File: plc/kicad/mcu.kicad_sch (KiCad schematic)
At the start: 26 parts, among them Q3 L8050QLT1G, Q4 L8050QLT1G, SW1 TSD003B08026A03, SW2 TSD003B08026A03, U10 CP2102N-A02-GQFN28R, U9 ESP32-S3-MINI-1U

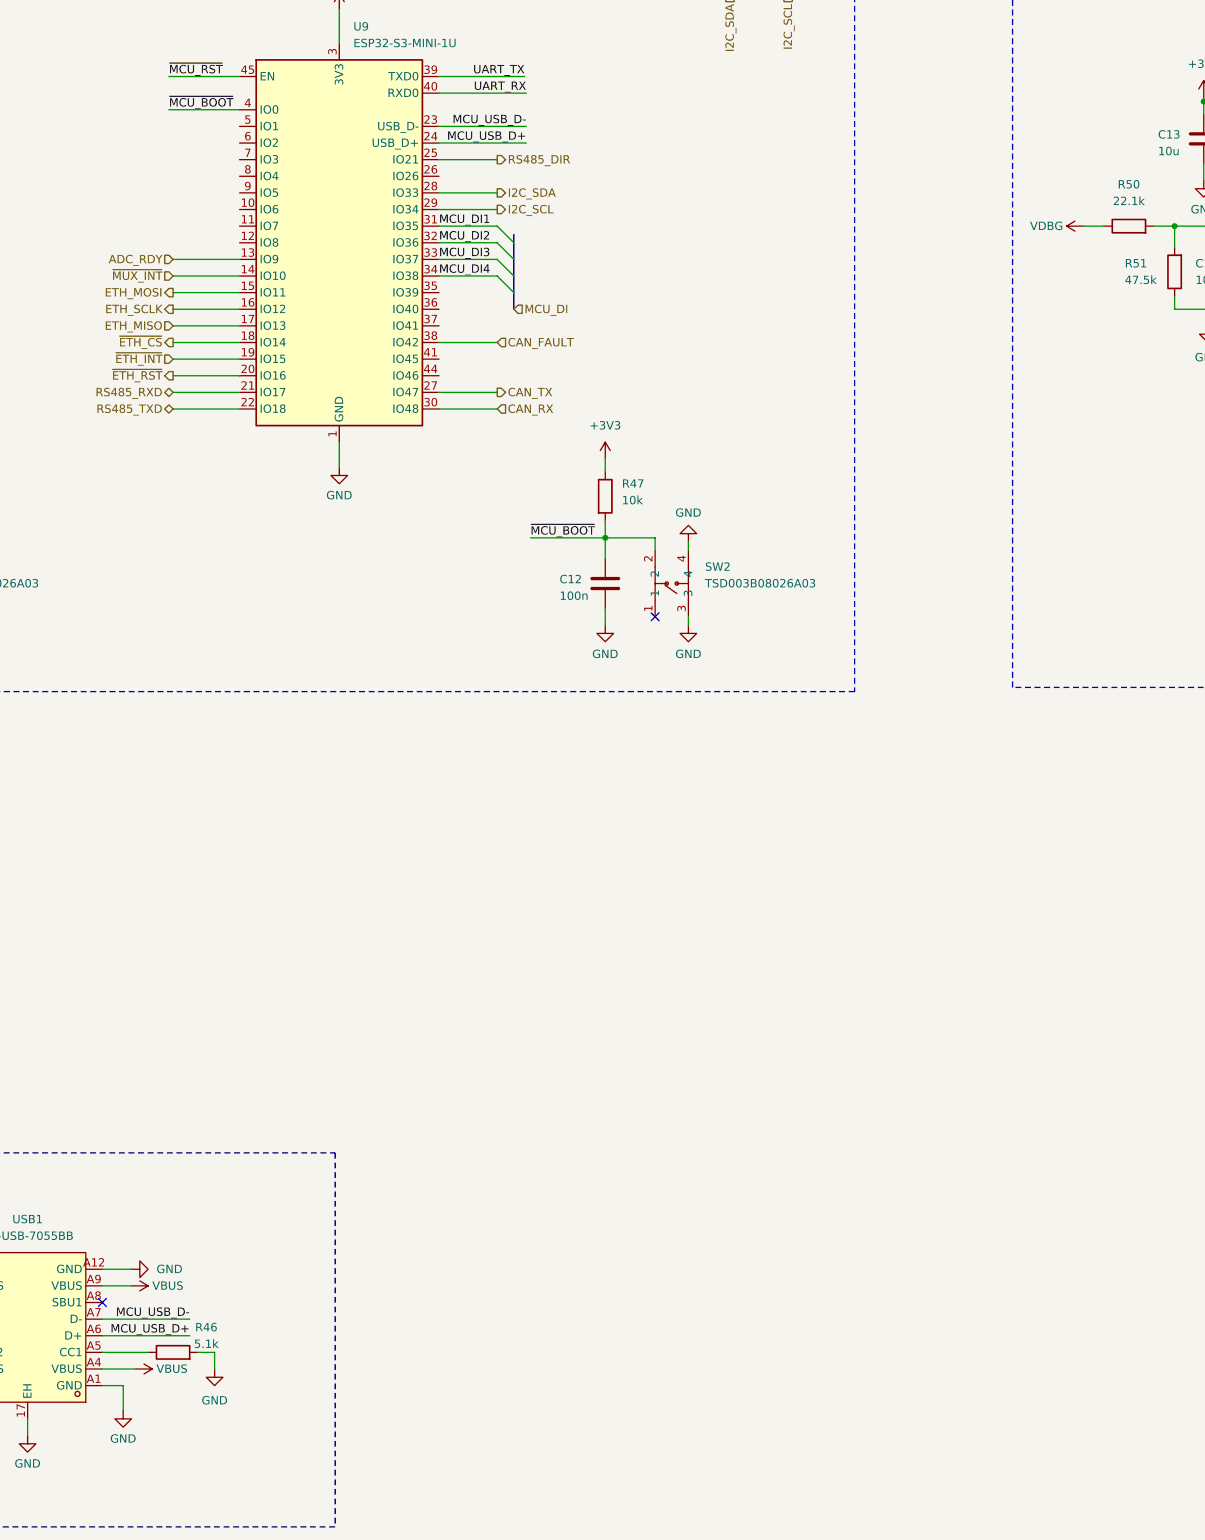
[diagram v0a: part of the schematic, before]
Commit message: AHT20 sensor added
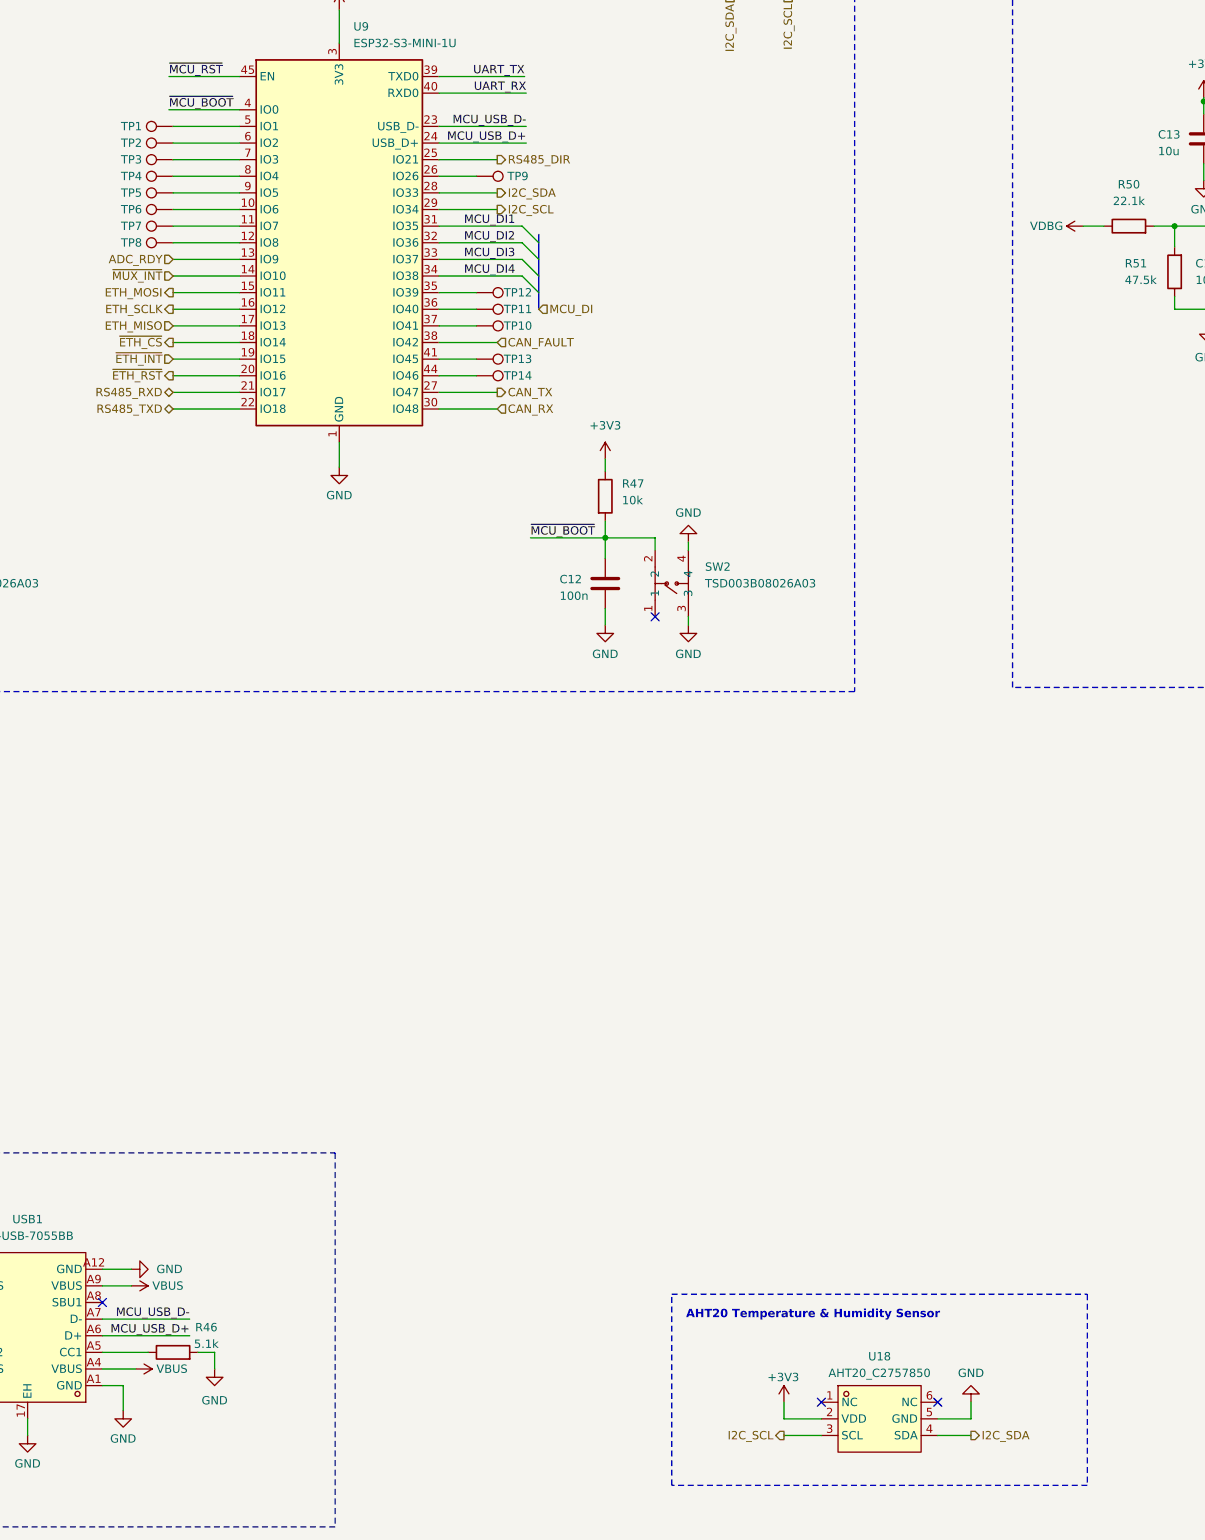
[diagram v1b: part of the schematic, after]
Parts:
- added TP1, TP10, TP11, TP12, TP13, TP14, TP2, TP3, TP4, TP5, TP6, TP7, TP8, TP9: TestPoint, TestPoint:TestPoint_Pad_D3.0mm, symbol Connector:TestPoint
- added U18: AHT20_C2757850, LibrePLC32:SENSOR-SMD_L3.0-W3.0-P1.00-BR, symbol LibrePLC32:AHT20_C2757850
- C11, C12, C13, C14: footprint Capacitor_SMD:C_0805_2012Metric -> Capacitor_SMD:C_0603_1608Metric
- R44, R47, R48, R49: footprint Resistor_SMD:R_0805_2012Metric -> Resistor_SMD:R_0603_1608Metric
- R45, R46, R50, R51, R52, R53, R54, R55, R56, R57: footprint Resistor_SMD:R_0805_2012Metric_Pad1.20x1.40mm_HandSolder -> Resistor_SMD:R_0603_1608Metric
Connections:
- net +3V3: now also U18.2 (VDD)
- net GND: now also U18.5 (GND)
- net I2C_SCL: now also U18.3 (SCL)
- net I2C_SDA: now also U18.4 (SDA)
- net at U9.10 (IO6): now also TP6.1
- net at U9.11 (IO7): now also TP7.1
- net at U9.12 (IO8): now also TP8.1
- net at U9.26 (IO26): now also TP9.1
- net at U9.35 (IO39): now also TP12.1
- net at U9.36 (IO40): now also TP11.1
- net at U9.37 (IO41): now also TP10.1
- net at U9.41 (IO45): now also TP13.1
- net at U9.44 (IO46): now also TP14.1
- net at U9.5 (IO1): now also TP1.1
- net at U9.6 (IO2): now also TP2.1
- net at U9.7 (IO3): now also TP3.1
- net at U9.8 (IO4): now also TP4.1
- net at U9.9 (IO5): now also TP5.1
- no-connect marks 22 -> 24
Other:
- note added: "AHT20 Temperature & Humidity Sensor"

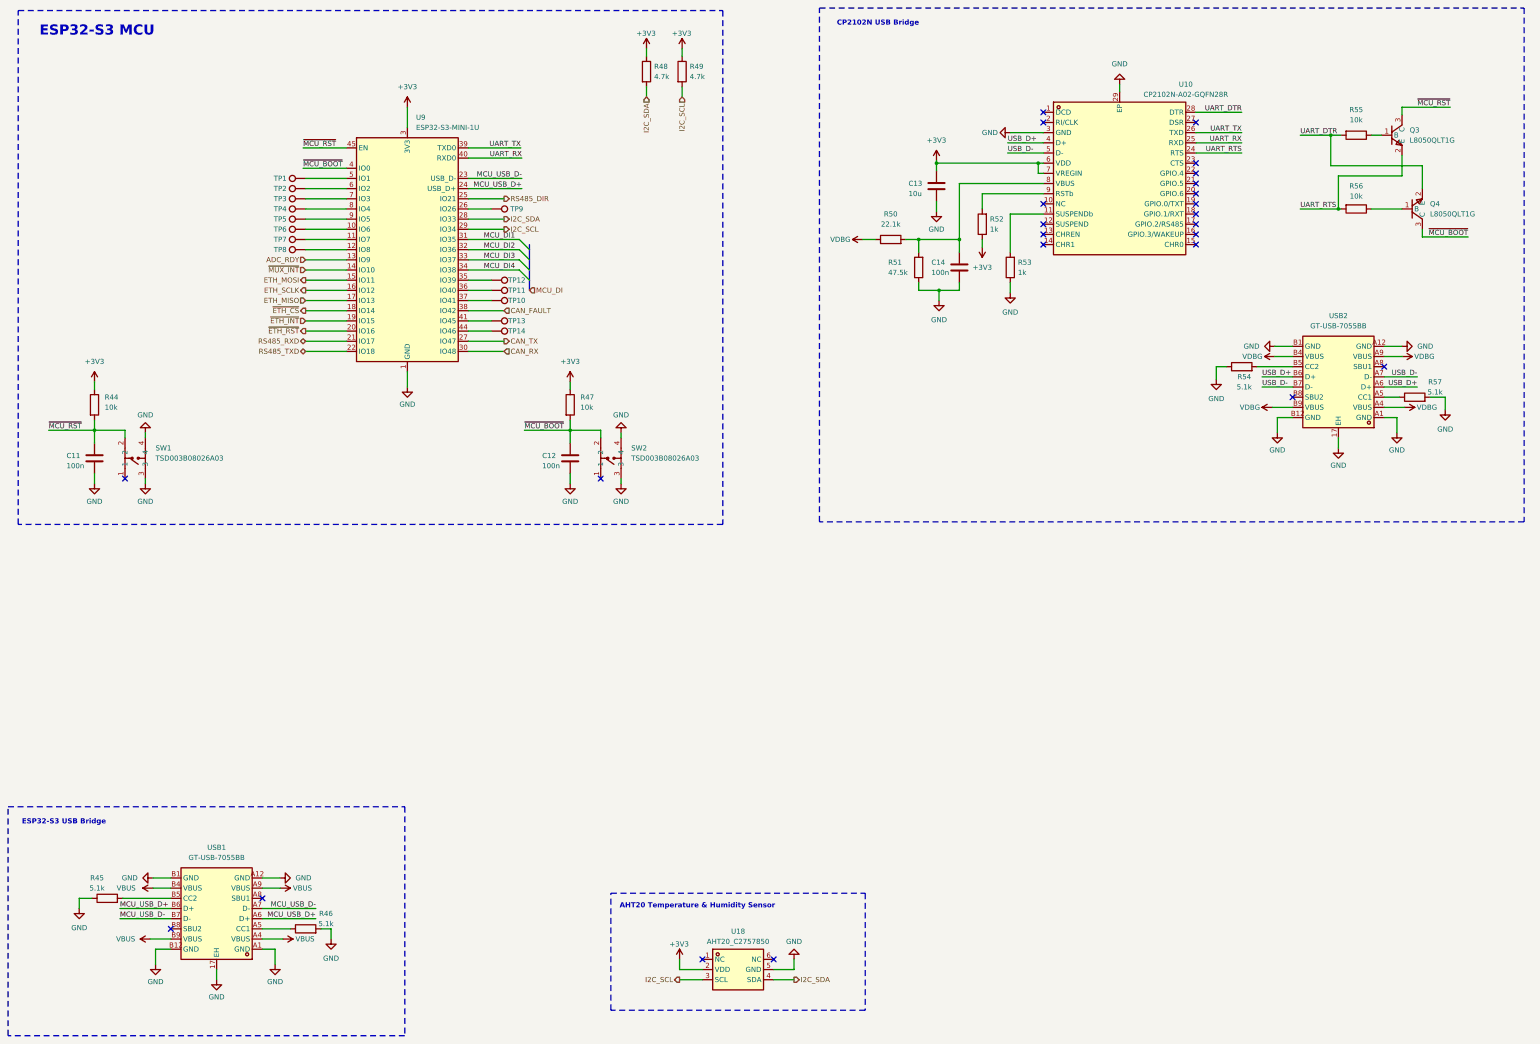
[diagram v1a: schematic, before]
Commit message: Added more testpads
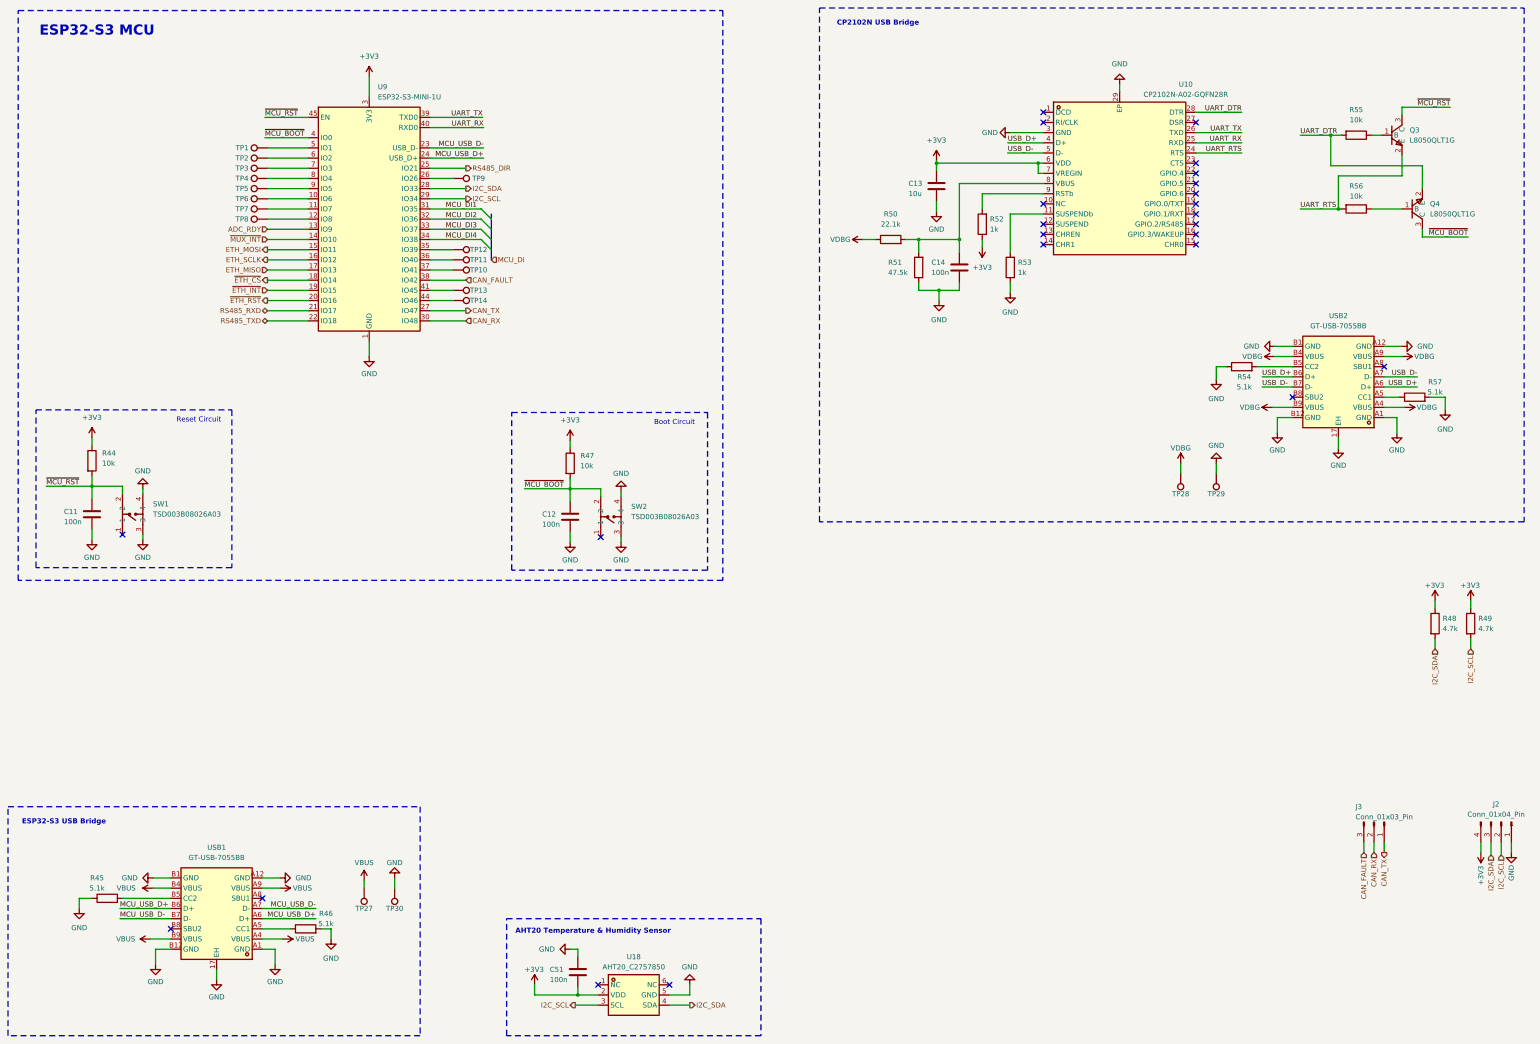
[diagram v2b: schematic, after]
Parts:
- added C51: 100n, Capacitor_SMD:C_0603_1608Metric, symbol Device:C
- added J2: Conn_01x04_Pin, Connector_PinSocket_2.54mm:PinSocket_1x04_P2.54mm_Vertical, symbol Connector:Conn_01x04_Pin
- added J3: Conn_01x03_Pin, symbol Connector:Conn_01x03_Pin
- added TP27, TP28, TP29, TP30: TestPoint, TestPoint:TestPoint_Pad_D3.0mm, symbol Connector:TestPoint
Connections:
- net +3V3: now also C51.1, J2.4 (Pin_4)
- net CAN_FAULT: now also J3.3 (Pin_3)
- net CAN_RX: now also J3.2 (Pin_2)
- net CAN_TX: now also J3.1 (Pin_1)
- net GND: now also C51.2, J2.1 (Pin_1), TP29.1, TP30.1
- net I2C_SCL: now also J2.2 (Pin_2)
- net I2C_SDA: now also J2.3 (Pin_3)
- net VBUS: now also TP27.1
- net VDBG: now also TP28.1
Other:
- note added: "Boot Circuit"
- note added: "Reset Circuit"
- moved on the sheet: C11, C12, R44, R47, R48, R49, SW1, SW2, TP1, TP10, TP11, TP12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

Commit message: Added RTC IC
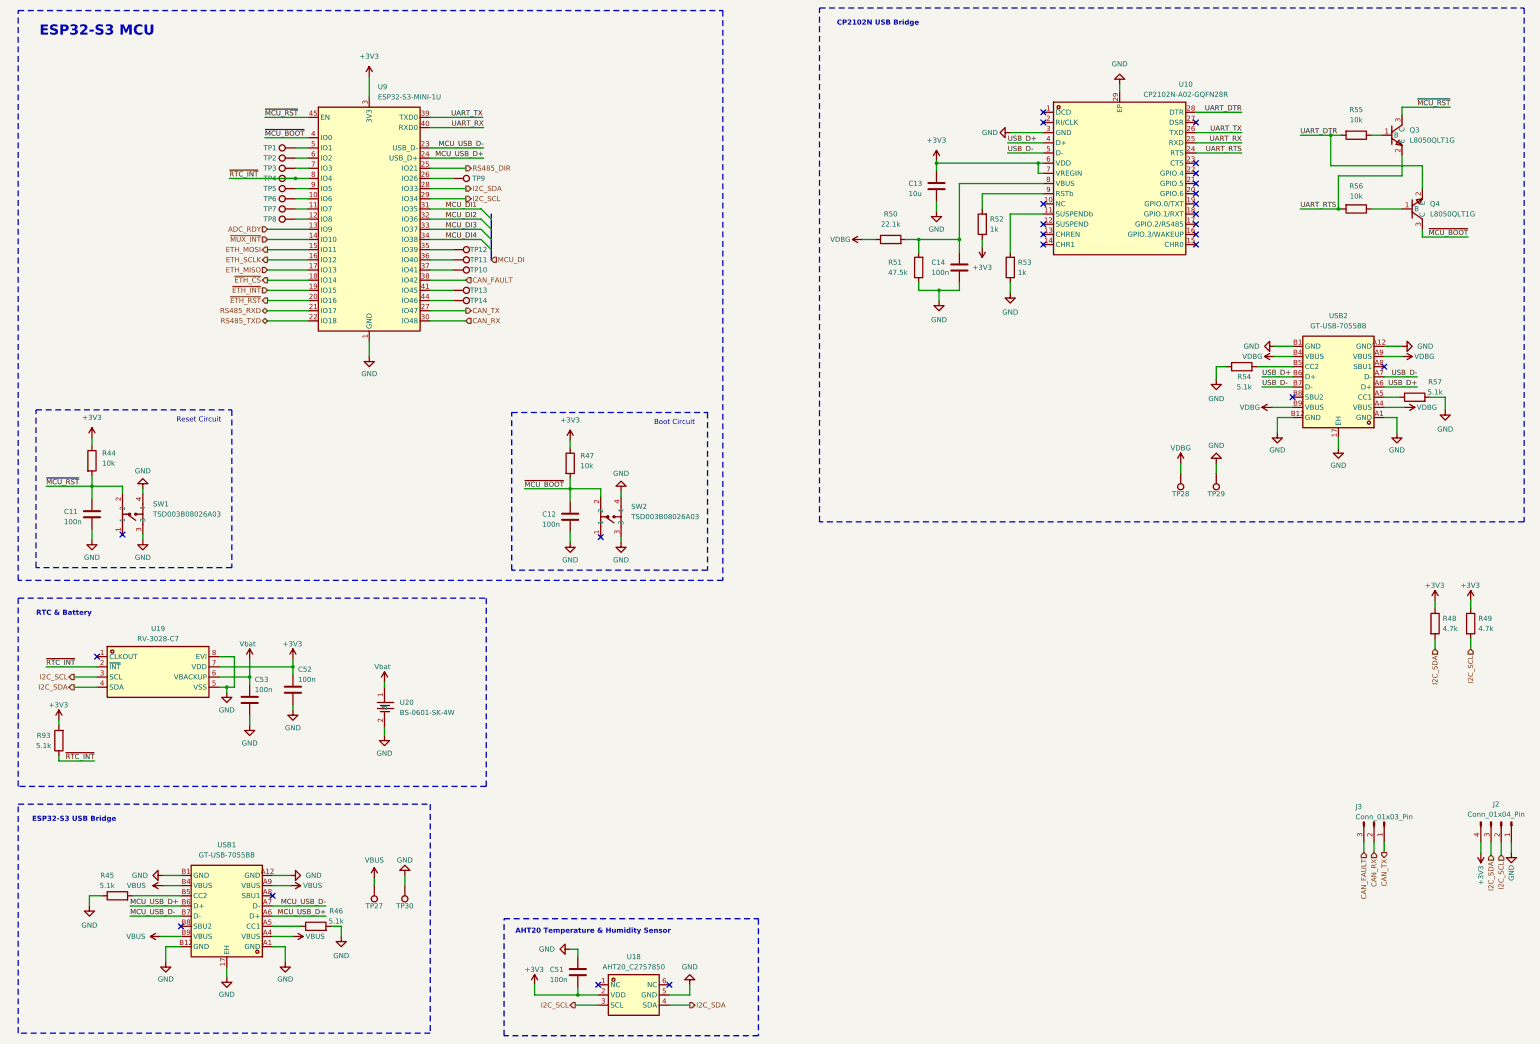
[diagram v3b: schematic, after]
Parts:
- added C52, C53: 100n, Capacitor_SMD:C_0603_1608Metric, symbol Device:C
- added R93: 5.1k, Resistor_SMD:R_0603_1608Metric, symbol Device:R
- added U19: RV-3028-C7, LibrePLC32:OSC-SMD_8P-L3.2-W1.5-P0.90-BL, symbol LibrePLC32:RV-3028-C732.768KHZ1PPMTAQC
- added U20: BS-0601-SK-4W, LibrePLC32:BAT-SMD_BS-06-B4AA012, symbol LibrePLC32:BS-0601-SK-4W
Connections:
- net +3V3: now also C52.2, R93.2, U19.7 (VDD)
- net GND: now also C52.1, C53.1, U19.5 (VSS), U19.8 (EVI), U20.2
- net I2C_SCL: now also U19.3 (SCL)
- net I2C_SDA: now also U19.4 (SDA)
- net ~{RTC_INT}: now reaches TP4.1, U9.8 (IO4)
- net ~{RTC_INT}: now also R93.1, U19.2 (~{INT})
- new net Vbat: C53.2, U19.6 (VBACKUP), U20.1
- no-connect marks 24 -> 25
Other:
- note added: "RTC & Battery"
- moved on the sheet: R45, R46, TP1, TP2, TP27, TP3, TP30, TP4, TP5, TP6, TP7, TP8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

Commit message: PCB placement
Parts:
- TP1, TP12, TP2, TP3, TP4, TP5, TP6, TP7, TP8: footprint TestPoint:TestPoint_Pad_D3.0mm -> TestPoint:TestPoint_Pad_D2.0mm
- TP11: renamed from TP9; footprint TestPoint:TestPoint_Pad_D3.0mm -> TestPoint:TestPoint_Pad_D2.0mm
- TP13: renamed from TP11; footprint TestPoint:TestPoint_Pad_D3.0mm -> TestPoint:TestPoint_Pad_D2.0mm
- TP14: renamed from TP10; footprint TestPoint:TestPoint_Pad_D3.0mm -> TestPoint:TestPoint_Pad_D2.0mm
- TP15: renamed from TP13; footprint TestPoint:TestPoint_Pad_D3.0mm -> TestPoint:TestPoint_Pad_D2.0mm
- TP16: renamed from TP14; footprint TestPoint:TestPoint_Pad_D3.0mm -> TestPoint:TestPoint_Pad_D2.0mm
- renumbered C53 to C12, C52 to C13, C12 to C14, C51 to C15, C13 to C16, C14 to C17, J3 to J1, R93 to R44, R44 to R45, R45 to R46, R46 to R47, R47 to R48, R50 to R49, R51 to R50, R52 to R51, R53 to R52, R54 to R53, R55 to R54, R56 to R55, R57 to R56, R48 to R57, R49 to R58, TP30 to TP10, TP28 to TP17, TP29 to TP18, TP27 to TP9, U9 to U10, U20 to U11, U18 to U12, U10 to U13, U19 to U9
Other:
- title: (none) -> LibrePLC32
